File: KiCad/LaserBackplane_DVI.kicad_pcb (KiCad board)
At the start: 2 copper layers, 69 x 28 mm, 47 parts, among them J1 Curr. Mod., J2 DVI-I, J5 Pz+, J6 Pz-, J7 Piezo_In, J8 Conn_Coaxial, K1 G6AU, Q1 MMBT3904, Q2 2N4401, U1 ADA4807-2ARM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

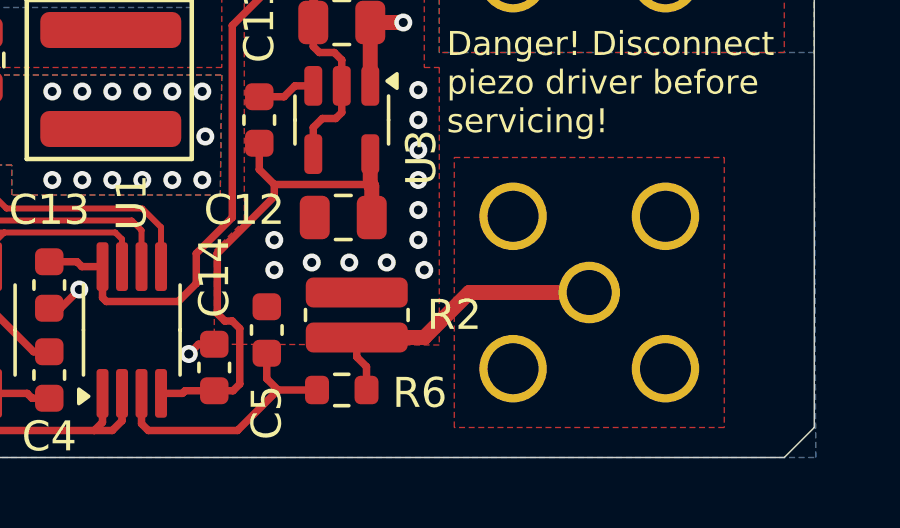
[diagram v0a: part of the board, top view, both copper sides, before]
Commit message: Replaced incorrect 3D model of the DVI connector (#12)
* Removed incorrect 3D model of the DVI connector

* Added 3D correct model of the DVI connector

* Replaced SMA connector footprint with correct one
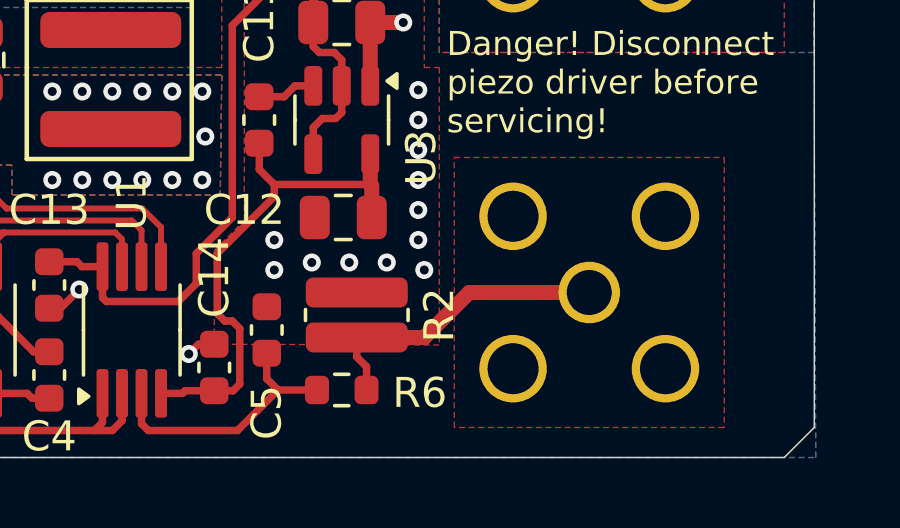
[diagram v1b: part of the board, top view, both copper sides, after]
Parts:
- J1, J7: footprint Connector_Coaxial:SMA_Amphenol_901-144_Vertical -> Connector_Coaxial:SMA_Amphenol_132291_Vertical

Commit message: Change R3 from 100k to 47k to increase the current through the relay during switch off
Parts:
- R3: value 100k -> 47k

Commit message: Bump to 1.8.1 (#17)
Updated authors
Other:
- board text added: "LaserBackplane v1.8.1 Design: T. Preuschoff, P. Baus Date: 2025-06 https://github.com/TU-Darmstadt-APQ/ Laser_Backplane_DVI"
- board text removed: "LaserBackplane v1.8.0 Design: T. Preuschoff, P. Baus Date: 2025-06 https://github.com/TU-Darmstadt-APQ/ Laser_Backplane_DVI"
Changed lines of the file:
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@@
 	(title_block
 		(title "Laser Backplane Diode DVI")
-		(date "2025-06-24")
-		(rev "1.8.0")
-		(company "APQ")
+		(date "2025-06-27")
+		(rev "1.8.1")
+		(company "Atoms-Photons-Quanta, TU Darmstadt and Quantum Electronic Devices GmbH")
 		(comment 1 "Tilman Preuschoff & Patrick Baus")
+		(comment 2 "Copyright (©) 2025, Patrick Baus <patrick.baus@quantum-electronic-devices.de>")
 	)
 	(layers
@@
 		)
 	)
-	(gr_text "LaserBackplane v1.8.0\nDesign: T. Preuschoff, P. Baus\nDate: 2025-06\nhttps://github.com/TU-Darmstadt-APQ/\nLaser_Backplane_DVI"
+	(gr_text "LaserBackplane v1.8.1\nDesign: T. Preuschoff, P. Baus\nDate: 2025-06\nhttps://github.com/TU-Darmstadt-APQ/\nLaser_Backplane_DVI"
 		(at 146.6 113.95 0)
 		(layer "B.SilkS")

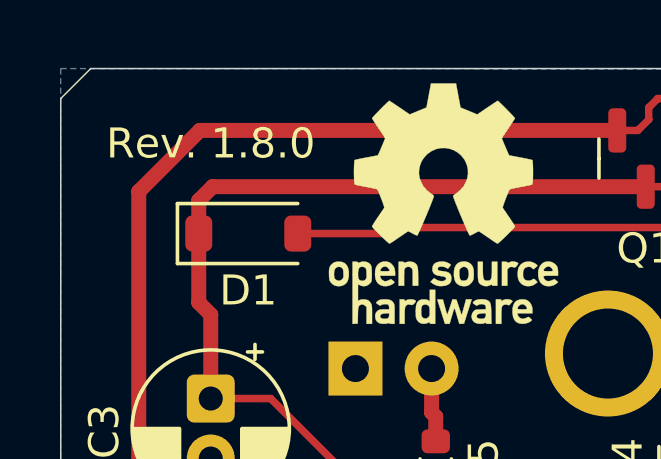
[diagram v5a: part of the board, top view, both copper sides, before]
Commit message: Fixed incorrect version label
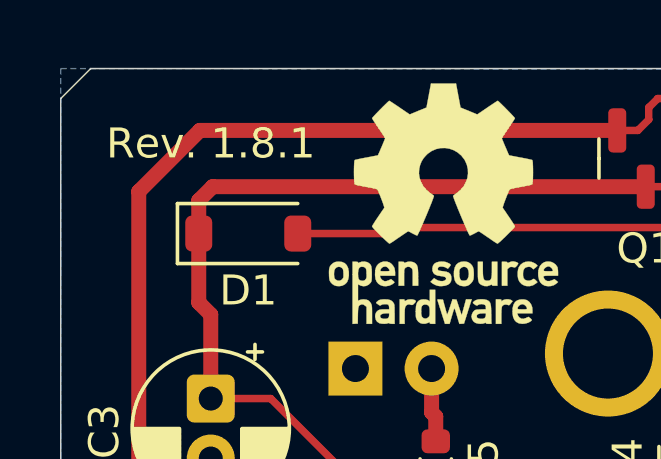
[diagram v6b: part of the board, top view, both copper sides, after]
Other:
- board text added: "Rev. 1.8.1"
- board text removed: "Rev. 1.8.0"
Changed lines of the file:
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@@
 		)
 	)
-	(gr_text "Rev. 1.8.0"
+	(gr_text "Rev. 1.8.1"
 		(at 95 92.5 0)
 		(layer "F.SilkS")
